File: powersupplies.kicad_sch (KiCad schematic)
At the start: 25 parts, among them U1 OB2222M, U2 STK17-3.3

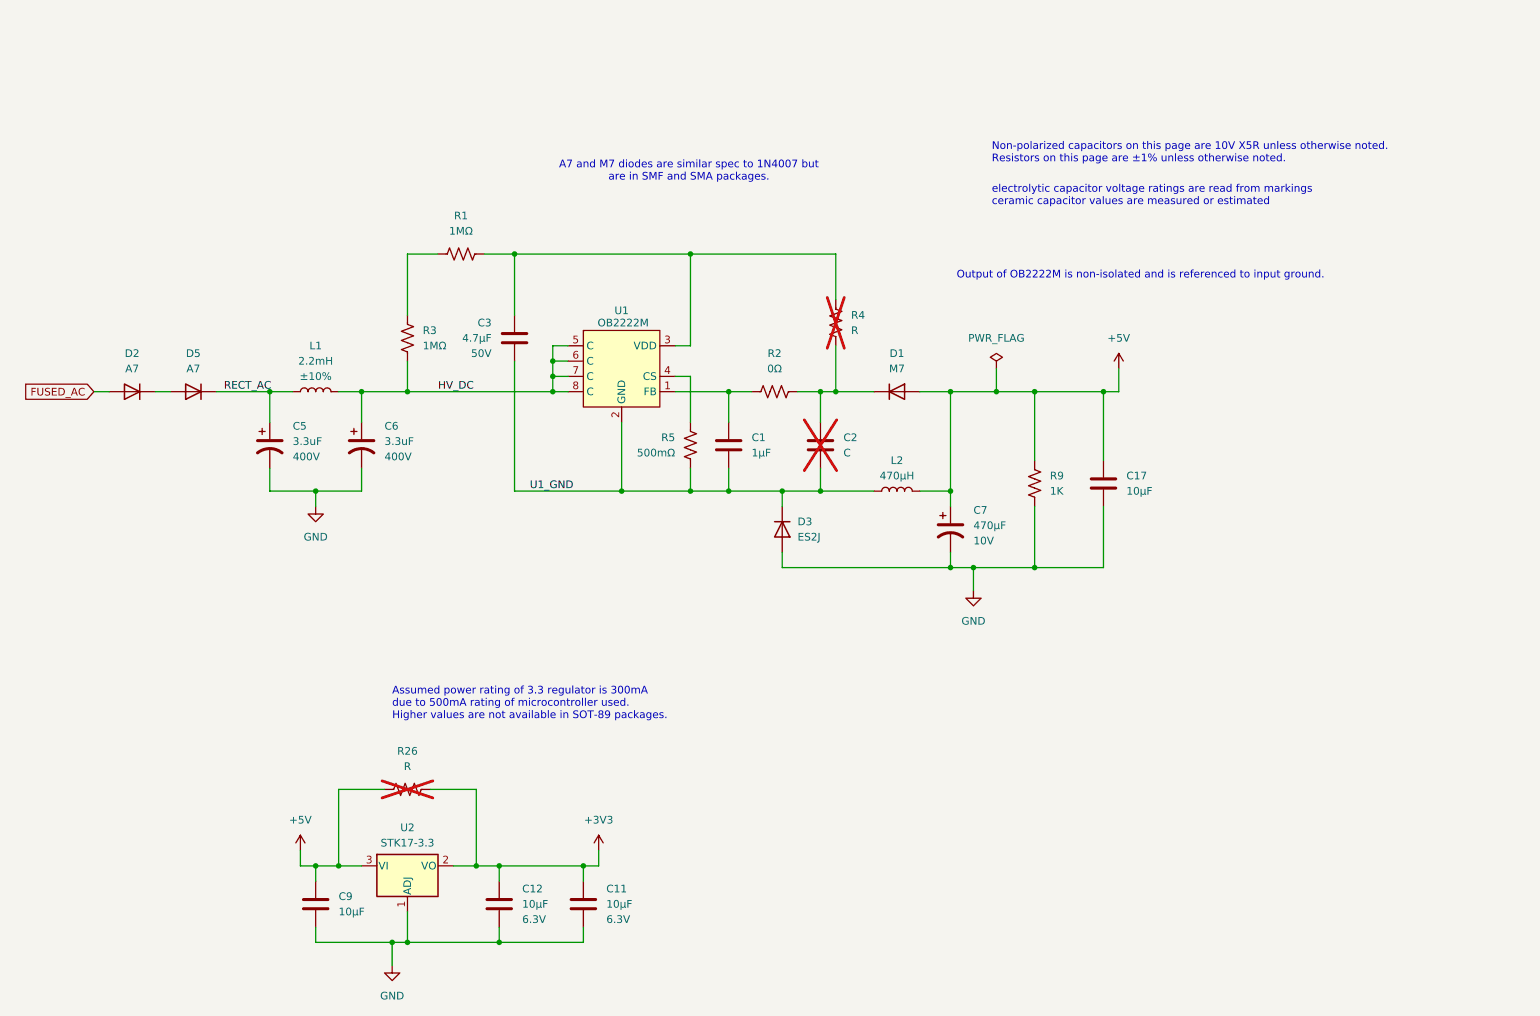
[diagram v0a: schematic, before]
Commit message: Rearranged SMPS circuit. Added a lot of schematic comments. Moved RECT_AC line away from NEUTRAL_SRC (not enough). Updated README greatly. Added pictures. Added PDF schematic.
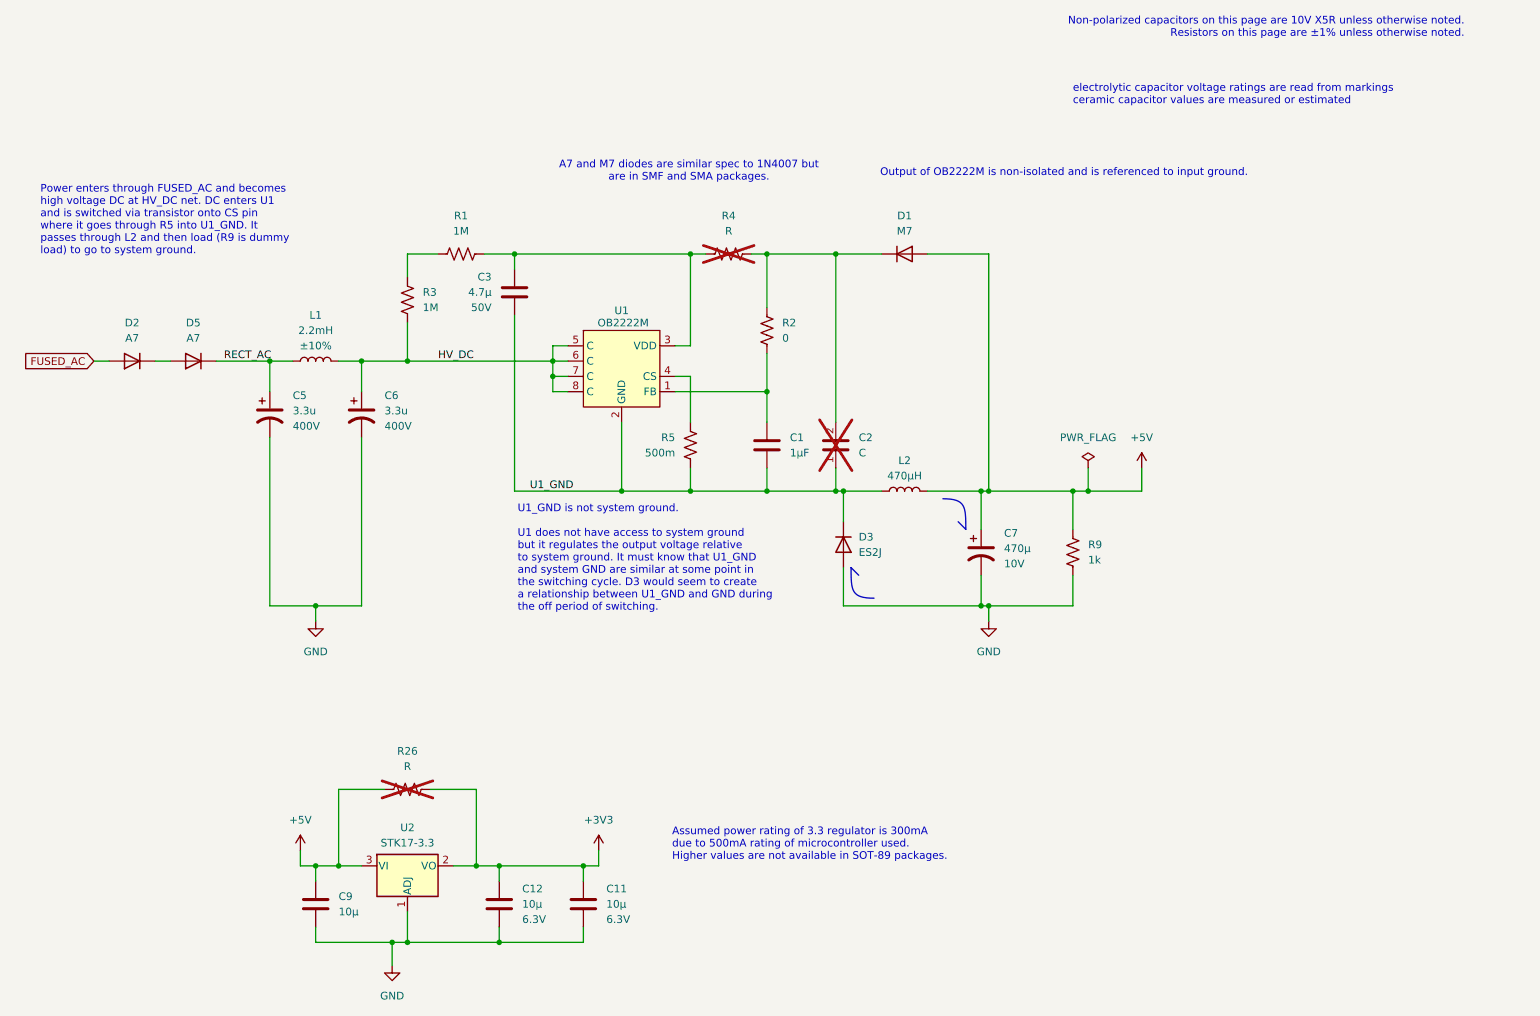
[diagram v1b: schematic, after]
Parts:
- removed C17: 10µF, Capacitor_SMD:C_0603_1608Metric, symbol Device:C
- C11, C12, C9: value 10µF -> 10µ
- C3: value 4.7µF -> 4.7µ
- C5, C6: value 3.3uF -> 3.3u
- C7: value 470µF -> 470µ
- R1, R3: value 1MΩ -> 1M
- R2: value 0Ω -> 0
- R5: value 500mΩ -> 500m
- R9: value 1K -> 1k
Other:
- note added: "Power enters through FUSED_AC and becomes high voltage DC at HV_DC net. DC enters U1 and is switched via transistor onto CS pin where it goes through R5 into U1_GND. It passes through L2 and then load (R9 is dummy load) to go to system ground."
- note added: "U1_GND is not system ground. U1 does not have access to system ground but it regulates the output voltage relative to system ground. It must know that U1_GND and system GND are similar at some point in the switching cycle. D3 would seem to create a relationship between U1_GND and GND during the off period of switching."
- moved on the sheet: C1, C3, C5, C6, C7, D1, D2, D3, D5, L1, L2, R2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
